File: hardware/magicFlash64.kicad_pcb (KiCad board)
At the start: 2 copper layers, 52.7 x 41.3 mm, 35 parts, among them J1 CONN_01X04, J2 Conn_01x07, J3 CONN_01X03, U1 ROMSOCKET, U2 ATMEGA48-20PU, U3 SST39SF040, Y1 20MHz

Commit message: pcb version 0.2
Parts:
- removed D7, D8, D9: D, Diodes_THT:D_DO-35_SOD27_P2.54mm_Vertical_AnodeUp
- removed JP6, JP7: Jumper_NC_Dual, Pin_Headers:Pin_Header_Straight_1x03_Pitch2.54mm
- added C4: 220p, Capacitors_THT:C_Disc_D3.4mm_W2.1mm_P2.50mm, F.Cu at (111.6, 93.1)
- added C5: 220p, Capacitors_THT:C_Disc_D3.4mm_W2.1mm_P2.50mm, F.Cu at (96.5, 104.1)
- added J4: 1x4, Pin_Headers:Pin_Header_Straight_1x04_Pitch2.54mm, F.Cu at (111.8, 73.4)
- added R10: 4.7K, Resistors_THT:R_Axial_DIN0204_L3.6mm_D1.6mm_P2.54mm_Vertical, F.Cu at (76.2, 75.7)
- added R11: 4.7K, Resistors_THT:R_Axial_DIN0204_L3.6mm_D1.6mm_P2.54mm_Vertical, F.Cu at (76.2, 78.2)
- added R12: 100, Resistors_THT:R_Axial_DIN0204_L3.6mm_D1.6mm_P2.54mm_Vertical, F.Cu at (98.9, 104.1)
- added R13: 270, Resistors_THT:R_Axial_DIN0204_L3.6mm_D1.6mm_P2.54mm_Vertical, F.Cu at (101.5, 106.9)
- J1: value CONN_01X04 -> 1x4
- J2: value Conn_01x07 -> 1x7
- J3: value CONN_01X03 -> 1x3
- JP1, JP2, JP3, JP5: value Jumper_NC_Dual -> 1x3
- JP4: value Jumper -> 1x2
- R9: value 2k -> 100
- U3: value SST39SF040 -> AM29F040
- moved R9 21.5 mm to (111.6, 90.8)
- moved J1 7.62 mm to (66.2, 72.6), turned to 0 degrees
- moved JP1 6.61 mm to (111.6, 98.7)
- moved JP4 6.43 mm to (105.4, 75.3)
- moved D1 0.63 mm to (76.2, 73.0)
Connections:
- J1 pad 2: RESTORE -> Net-(J1-Pad2)
- J1 pad 3: NET -> RW
- J1 pad 4: RW -> GPIO
- JP1 pad 1: OE -> GND
- JP1 pad 2: OE_A11 -> GND_A11
- R9 pad 1: GND -> Net-(C4-Pad1)
- R9 pad 2: Net-(D7-Pad1) -> OE
- U1 pad 20: GND -> GND_A11
- U1 pad 22: OE_A11 -> OE
- U2 pad 14: RW -> Net-(C5-Pad2)
- U2 pad 17: OE -> Net-(C4-Pad1)
- U2 pad 19: OE_EN -> GPIO
- U2 pad 2: NET -> Net-(J4-Pad3)
- U3 pad 1: Net-(JP6-Pad2) -> SEL_A18
- U3 pad 24: Net-(D7-Pad1) -> Net-(C4-Pad1)
- U3 pad 30: Net-(JP7-Pad2) -> SEL_A17
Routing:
- net Net-(J1-Pad2): track 0.00 -> 75.8 mm, vias 0 -> 2
- net Net-(C4-Pad1): track 0.00 -> 48.7 mm, vias 0 -> 1
- net Net-(J4-Pad4): track 2.80 -> 50.7 mm, vias 0 -> 1
- net Net-(J4-Pad3): track 0.00 -> 46.7 mm, vias 0 -> 2
- net OE: track 42.9 -> 3.31 mm
- net Net-(JP6-Pad2): track 39.6 -> 0.00 mm
- net GPIO: track 0.00 -> 30.6 mm
- net RESTORE: track 18.5 -> 44.3 mm, vias 0 -> 3
- net OE_EN: track 24.7 -> 0.00 mm
- net Net-(D7-Pad1): track 21.5 -> 0.00 mm
- net Net-(C5-Pad2): track 0.00 -> 21.1 mm
- net NET: track 18.7 -> 0.00 mm
- net RW: track 54.4 -> 71.4 mm
- net Net-(JP7-Pad2): track 10.2 -> 0.00 mm
- net SEL_A18: track 80.3 -> 71.0 mm
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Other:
- board text added: "magicFlash64 - by zschunky - v0.2"
- board text removed: "magicFlash64 - by zschunky - v0.1"

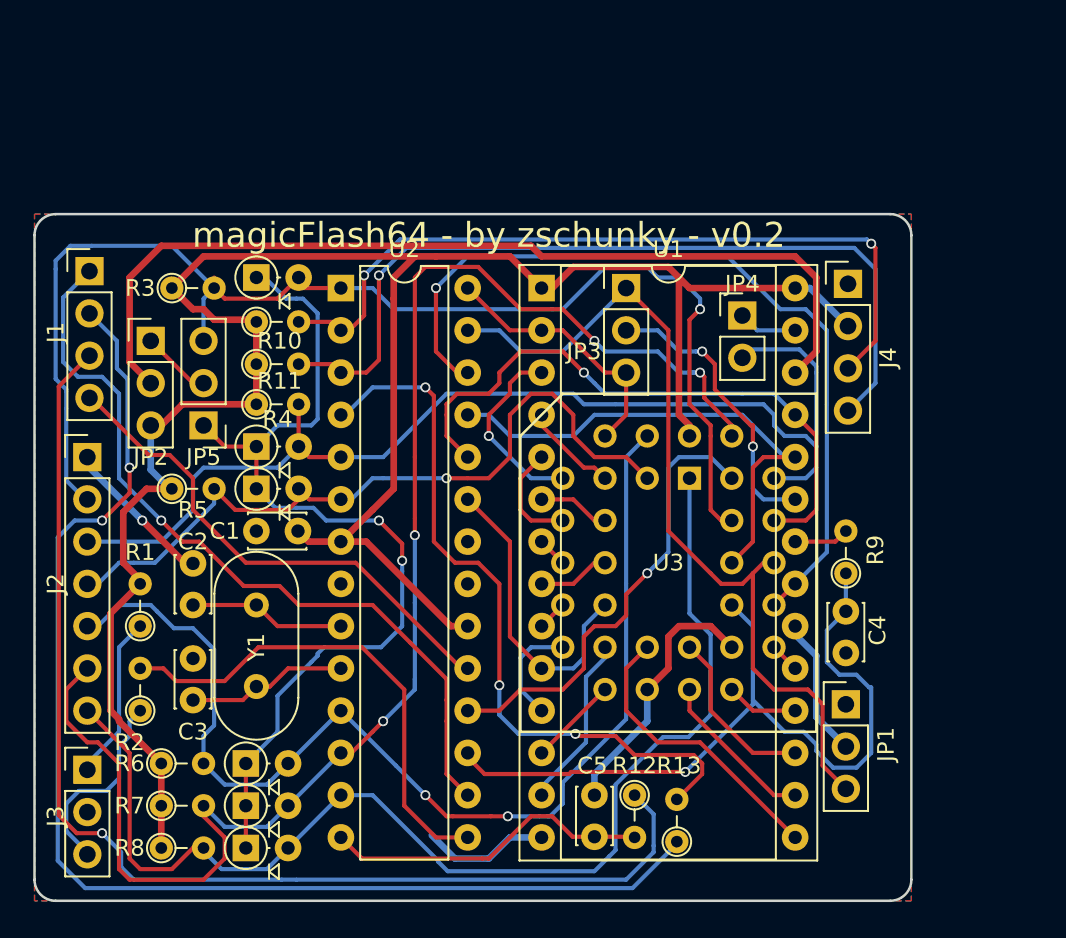
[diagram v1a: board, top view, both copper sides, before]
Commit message: added pcb v0.3 which uses external clock via c64 dot clock
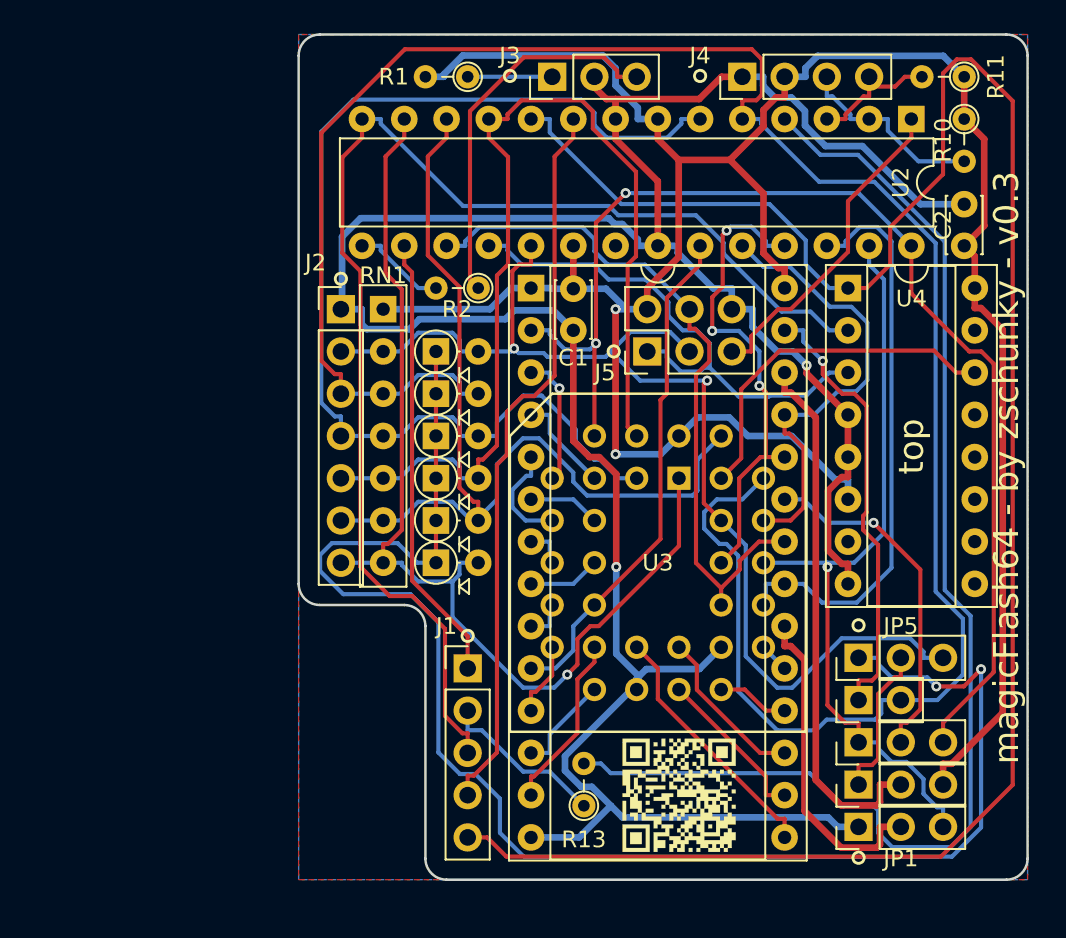
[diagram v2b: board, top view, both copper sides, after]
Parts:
- removed C3: 22p, Capacitors_THT:C_Disc_D3.4mm_W2.1mm_P2.50mm
- removed C4, C5: 220p, Capacitors_THT:C_Disc_D3.4mm_W2.1mm_P2.50mm
- removed R12, R9: 100, Resistors_THT:R_Axial_DIN0204_L3.6mm_D1.6mm_P2.54mm_Vertical
- removed R3, R4: 10k, Resistors_THT:R_Axial_DIN0204_L3.6mm_D1.6mm_P2.54mm_Vertical
- removed R5, R6, R7, R8: 10K, Resistors_THT:R_Axial_DIN0204_L3.6mm_D1.6mm_P2.54mm_Vertical
- removed Y1: 20MHz, Crystals:Crystal_HC18-U_Vertical
- added G***: LOGO, zschunkyFootprints:qrcode, F.Cu at (101.6, 104.1)
- added J5: AVR ISP, Pin_Headers:Pin_Header_Straight_2x03_Pitch2.54mm, F.Cu at (99.7, 77.5)
- added RN1: 10k, Resistors_THT:R_Array_SIP7, F.Cu at (83.8, 74.9)
- added U4: 74LS138, Housings_DIP:DIP-16_W7.62mm_Socket, F.Cu at (111.8, 73.7)
- C2: value 22p -> 100n
- J1: value 1x4 -> 1x5; footprint Pin_Headers:Pin_Header_Straight_1x04_Pitch2.54mm -> Pin_Headers:Pin_Header_Straight_1x05_Pitch2.54mm
- moved C2 51.1 mm to (118.7, 71.1)
- moved JP2 50.2 mm to (112.4, 103.5), turned to 90 degrees
- moved J3 50.2 mm to (94.0, 61.0), turned to 90 degrees
- moved R11 45.9 mm to (118.7, 61.0), turned to 180 degrees
- moved R10 44.3 mm to (118.7, 63.5), turned to 270 degrees
- moved JP5 41.8 mm to (112.4, 95.9), turned to 90 degrees
- moved R1 38.4 mm to (88.9, 61.0), turned to 180 degrees
- moved U2 35.8 mm to (115.6, 63.5), turned to 270 degrees
- moved J1 33.0 mm to (88.9, 96.5)
- moved R2 32.5 mm to (89.5, 73.7), turned to 180 degrees
- moved JP3 30.7 mm to (112.4, 101.0), turned to 90 degrees
- moved JP4 24.1 mm to (112.4, 98.4), turned to 90 degrees
- moved C1 22.5 mm to (95.2, 76.2), turned to 90 degrees
- moved D5 20.6 mm to (87.0, 87.6)
- moved D4 20.6 mm to (87.0, 85.1)
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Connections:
- net Net-(J4-Pad3) renamed /SCL
- net Net-(J4-Pad4) renamed /SDA
- C2 pad 1: Net-(C2-Pad1) -> VCC
- D1 pad 2: SEL_A13 -> SCK
- J1 pad 4: GPIO -> DOT_CLK
- J2 pad 2: SEL_A13 -> SCK
- JP5 pad 3: SEL_A13 -> SCK
- U1 pad 22: OE -> MOSI
- U2 pad 1: SEL_A13 -> RST
- U2 pad 10: Net-(C3-Pad1) -> PHI2
- U2 pad 14: Net-(C5-Pad2) -> RW
- U2 pad 17: Net-(C4-Pad1) -> MOSI
- U2 pad 18: WE -> MISO
- U2 pad 19: GPIO -> SCK
- U2 pad 9: Net-(C2-Pad1) -> DOT_CLK
- U3 pad 24: Net-(C4-Pad1) -> MOSI
- U3 pad 28: SEL_A13 -> SCK
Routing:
- net GND: track 33.0 -> 168.1 mm, vias 1 -> 2
- net PHI2: track 0.00 -> 122.2 mm
- net SEL_A13: track 77.6 -> 0.00 mm, vias 1 -> 0
- net SCK: track 0.00 -> 69.7 mm, vias 0 -> 2
- net SEL_A14: track 67.3 -> 133.6 mm
- net Net-(J1-Pad2): track 75.8 -> 10.0 mm, vias 2 -> 0
- net A12: track 16.0 -> 72.1 mm, vias 0 -> 2
- net Net-(C4-Pad1): track 48.7 -> 0.00 mm, vias 1 -> 0
- net DOT_CLK: track 0.00 -> 43.9 mm
- net /SDA: track 50.7 -> 7.86 mm, vias 1 -> 0
- net MOSI: track 0.00 -> 42.4 mm
- net LOROM: track 56.5 -> 93.0 mm
- net /SCL: track 46.7 -> 11.6 mm, vias 2 -> 0
- net SEL_A17: track 92.3 -> 57.7 mm, vias 4 -> 0
- net MISO: track 0.00 -> 32.0 mm
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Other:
- board size 52.7 x 41.3 mm -> 43.8 x 50.8 mm
- board text added: "24pin"
- board text added: "28pin"
- board text added: "28pin kernal 24pin kernal"
- board text added: "JP1 1-2 2-3"
- board text added: "JP2 1-2 2-3"
- board text added: "JP3 1-2 2-3"
- board text added: "JP4 open open"
- board text added: "JP5 1-2 1-2"
- board text added: "bottom"
- board text added: "magicFlash64 - by zschunky - v0.3"
- board text added: "top"
- board text added: "°"
- board text removed: "magicFlash64 - by zschunky - v0.2"
